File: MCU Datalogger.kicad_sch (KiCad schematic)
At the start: 25 parts, among them U1 24LC1025, U2 DS1337S_, U3 24LC1025, U4 ATMEGA328P-AU, Y1 32.768 KHZ, Y2 16 MHZ

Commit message: Wiring of first sheet
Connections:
- net GND: now reaches C1.1
- net GND: now also BT1.2 (-), C2.1, C3.2, C4.2, C5.2, R1.2, R2.2, R7.2, U1.4 (GND), U1.7 (WP), U2.4 (GND), U3.2 (A1), U3.4 (GND), U3.7 (WP), U4.21 (GND), U4.3 (GND), U4.5 (GND)
- net at C1.2: now also U4.8 (PB7(PCINT7/XTAL2/TOSC2)), Y2.1
- net at Y1.1: now also U2.2 (X2)
- net at Y1.2: now also U2.1 (X1)
- net vcc: now reaches C3.1
- net vcc: now also R3.1, R4.1, R5.1, R6.1, U1.1 (A0), U1.2 (A1), U1.3 (A2), U1.8 (VCC), U2.8 (VCC), U3.1 (A0), U3.3 (A2), U3.8 (VCC)
- net at D1.1 (K): now also R2.1
- net SCK: now reaches D1.2 (A)
- net SCK: now also R4.2, U1.6 (SCL), U2.6 (SCL), U3.6 (SCL), U4.17 (PB5(SCK/PCINT5)), U4.28 (PC5(ADC5/SCL/PCINT13))
- net at D2.1 (K): now also R7.1
- net at D2.2 (A): now also BT1.1 (+), C5.1, U4.18 (AVCC), U4.4 (VCC)
- net at C2.2: now also U4.7 (PB6(PCINT6/XTAL1/TOSC1)), Y2.2
- net at R6.2: now also U2.3 (~{INTA})
- net at C4.1: now also U4.20 (AREF)
- net RESET: now reaches R1.1
- net RESET: now also U4.29 (PC6(*RESET/PCINT14))
- net SDA: now reaches U3.5 (SDA)
- net SDA: now also R3.2, U1.5 (SDA), U2.5 (SDA), U4.27 (PC4(ADC4/SDA/PCINT12))
- net D3: now reaches U4.1 (PD3(PCINT19/OC2B/INT1))
- net D6: now reaches U4.10 (PD6(PCINT22/OC0A/AIN0))
- net D7: now reaches U4.11 (PD7(PCINT23/AIN1))
- net D8: now reaches U4.12 (PB0(PCINT0/CLKO/ICP1))
- net MOSI: now reaches U4.15 (PB3(PCINT3/OC2A/MOSI))
- net MISO: now reaches U4.16 (PB4(PCINT4/MISO))
- net D4: now reaches U4.2 (PD4(PCINT20/XCK/T0))
- net RX: now reaches U4.30 (PD0(RXD/PCINT16))
- net TX: now reaches U4.31 (PD1(TXD/PCINT17))
- net D2: now reaches U4.32 (PD2(INT0/PCINT18))
- net D5: now reaches U4.9 (PD5(PCINT21/OC0B/T1))
- net at R5.2: now also U2.7 (SQW/~INT)
- no-connect marks 0 -> 9
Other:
- moved on the sheet: C1, C2, C4, D1, R1, R2, U4, Y1

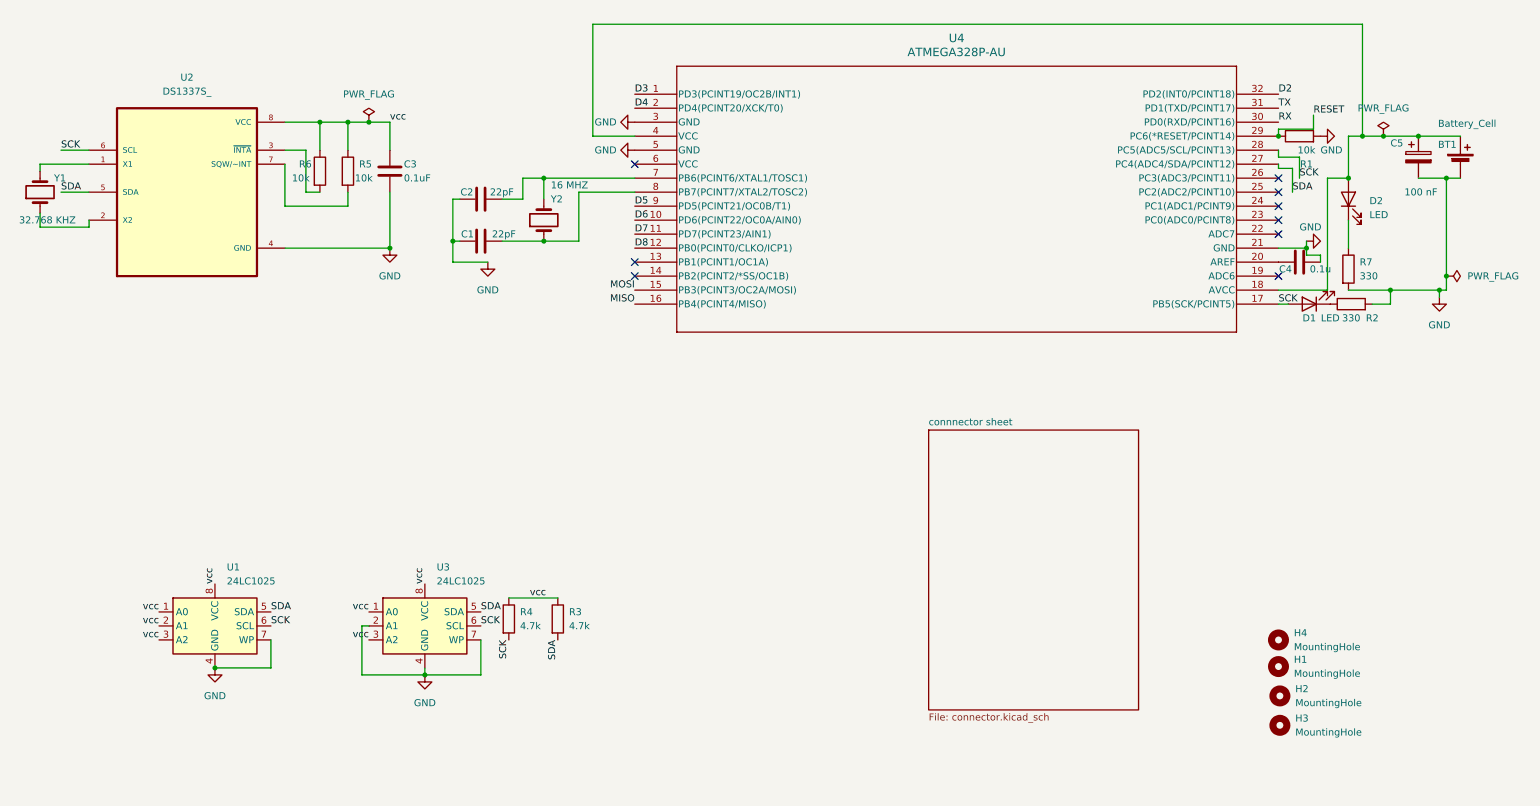
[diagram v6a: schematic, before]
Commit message: COMPLETED THE WIRING AND RESOLVED ERC ERRORS SUCH AS POWER PIN ASSIGNMENT AND THE MCU UNIT SYMBOL TYPE(INPUT,OUTPUT,PASSIVE ETC
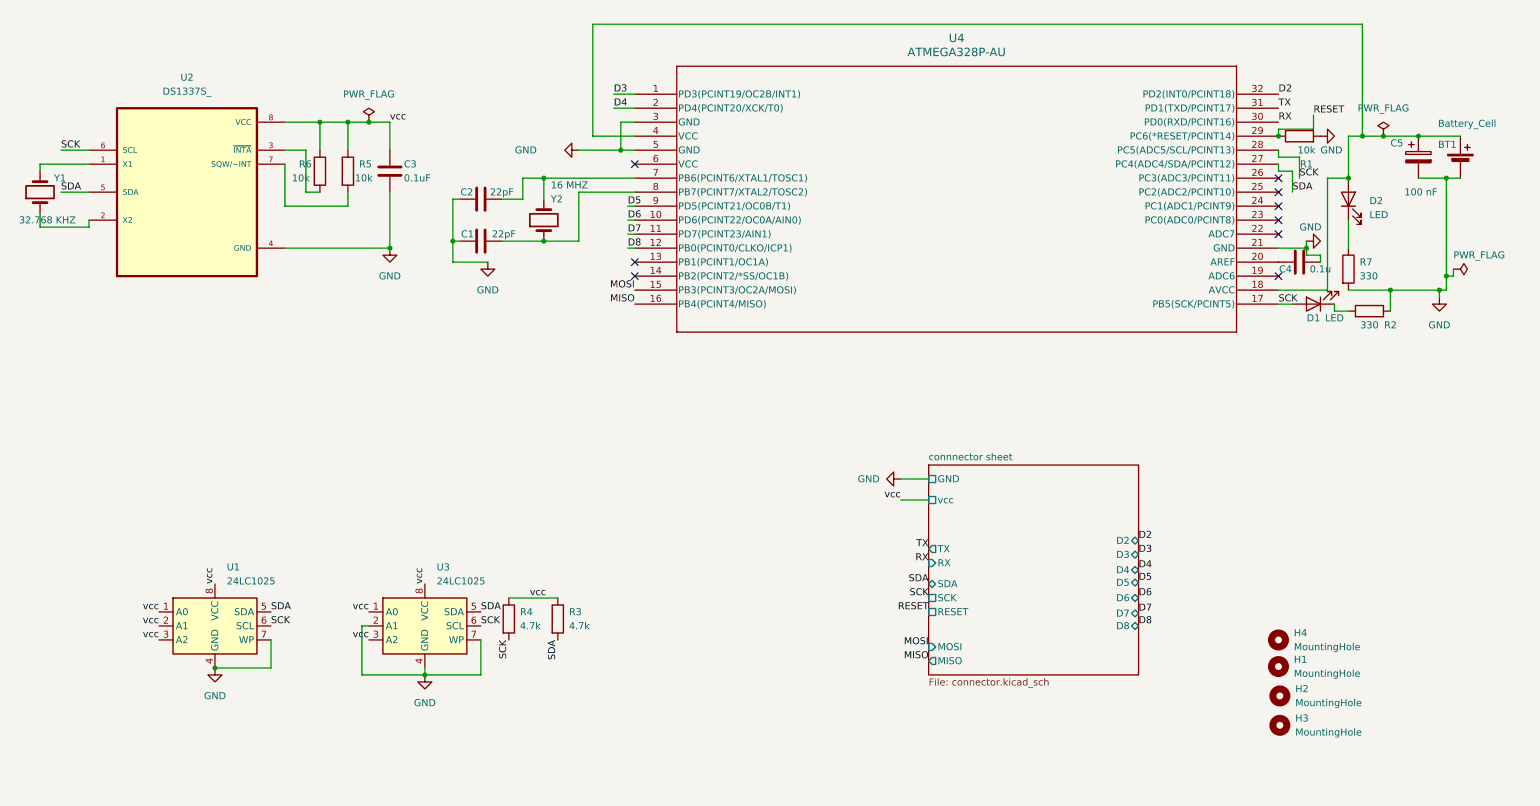
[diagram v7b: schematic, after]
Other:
- sheet connnector sheet ports: added D2, D3, D4, D5, D6, D7, D8, GND, MISO, MOSI, RESET, RX, SCK, SDA, TX, vcc; removed none
- moved on the sheet: D1, R2

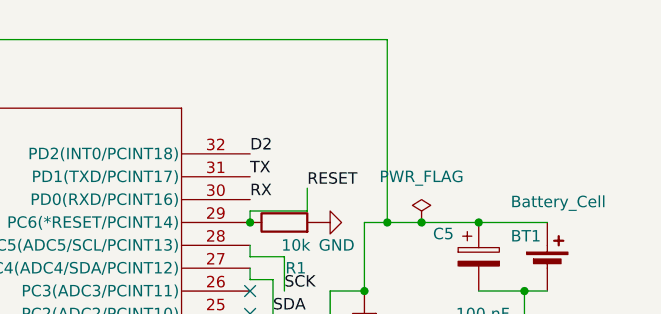
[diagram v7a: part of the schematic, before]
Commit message: arranged route track and later the schematics there was small mistkae so arranged and routed successfully preparation for manufacturing
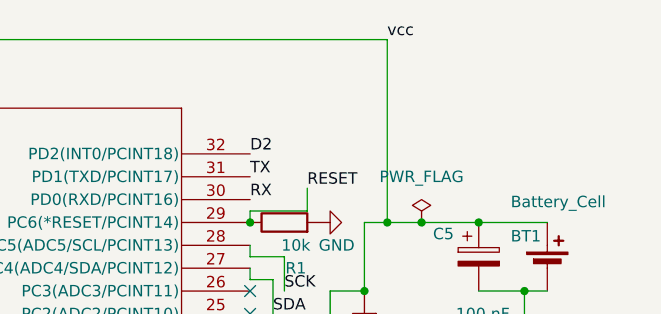
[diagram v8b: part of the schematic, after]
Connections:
- net vcc: now also BT1.1 (+), C5.1, D2.2 (A), U4.18 (AVCC), U4.4 (VCC)
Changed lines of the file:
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@@
+		)
+	)
+	(label "vcc"
+		(at 256.54 15.24 0)
+		(effects
+			(font
+				(size 1.27 1.27)
+			)
+			(justify left bottom)
 		)
 	)
